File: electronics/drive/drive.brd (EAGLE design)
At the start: 35 x 25 mm, 11 parts, among them IC1 MEGA8-AI, IC2 MAX1483ESA, J1 AVR_SPI_PRG_6NS

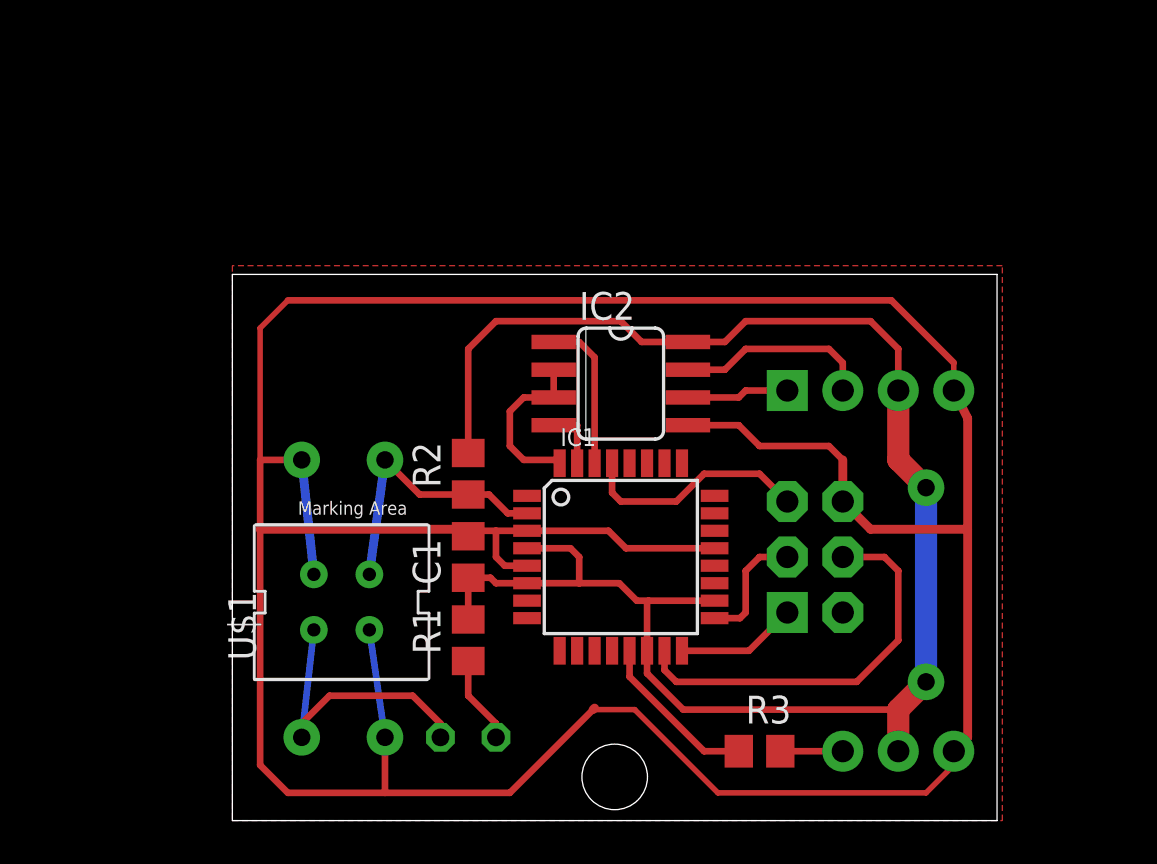
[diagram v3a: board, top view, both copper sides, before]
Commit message: Editing the board based on the build experiences :-)
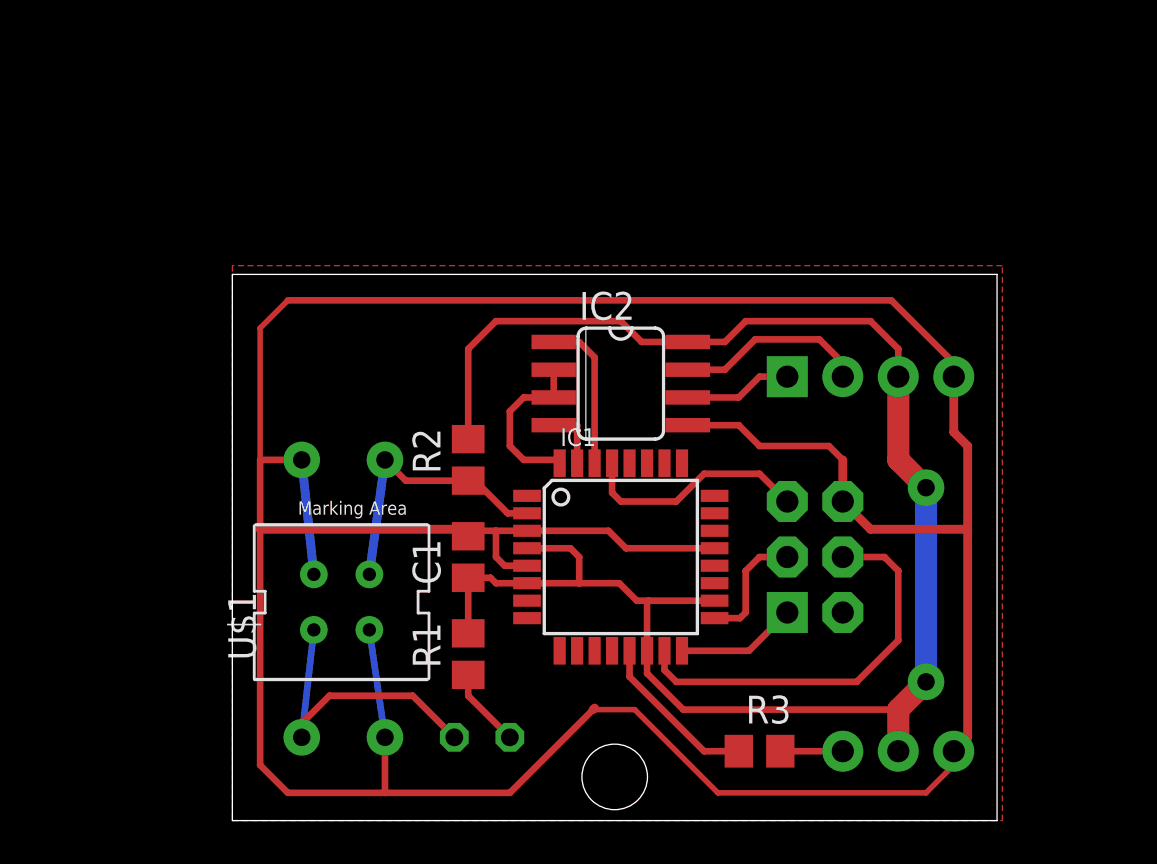
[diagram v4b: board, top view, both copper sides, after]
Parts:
- moved JP1 0.64 mm to (25.4, 20.3)
- moved R2 0.64 mm to (10.8, 16.5)
- moved R1 0.64 mm to (10.8, 7.62)
- moved LED1 0.63 mm to (11.4, 3.81)
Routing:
- net +5V: track 80.3 -> 79.6 mm
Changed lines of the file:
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@@
 <attribute name="NAME" x="1.079" y="7.333" size="1.27" layer="25" ratio="10" rot="R90"/>
 </element>
-<element name="LED1" library="led" package="LED3MM" value="3MM RED / 20mA, 1.8V" x="10.795" y="3.81" rot="MR0"/>
-<element name="R1" library="rcl" package="R0805" value="200" x="10.795" y="8.255" rot="R90"/>
+<element name="LED1" library="led" package="LED3MM" value="3MM RED / 20mA, 1.8V" x="11.43" y="3.81" rot="MR0"/>
+<element name="R1" library="rcl" package="R0805" value="200" x="10.795" y="7.62" rot="R90"/>
 <element name="C1" library="rcl" package="C0805" value="100nF" x="10.795" y="12.065" rot="R90"/>
-<element name="JP1" library="SparkFun" package="MOLEX-1X4" value="" x="25.4" y="19.685" rot="MR180"/>
+<element name="JP1" library="SparkFun" package="MOLEX-1X4" value="" x="25.4" y="20.32" rot="MR180"/>
 <element name="JP2" library="SparkFun" package="1X03" value="" x="33.02" y="3.175" rot="MR0"/>
 <element name="IC1" library="atmel" package="TQFP32-08" value="MEGA8-AI" x="17.78" y="12.065">
@@
 </element>
 <element name="J1" library="SparkFun" package="2X3-NS" value="AVR_SPI_PRG_6NS" x="26.67" y="12.065" rot="MR90"/>
-<element name="R2" library="rcl" package="R0805" value="12k" x="10.795" y="15.875" rot="R90"/>
+<element name="R2" library="rcl" package="R0805" value="12k" x="10.795" y="16.51" rot="R90"/>
 <element name="R3" library="rcl" package="R0805" value="1k" x="24.13" y="3.175"/>
 </elements>
@@
 <wire x1="18.415" y1="5.08" x2="22.225" y2="1.27" width="0.254" layer="1"/>
 <wire x1="16.51" y1="5.08" x2="18.415" y2="5.08" width="0.254" layer="1"/>
-<wire x1="33.02" y1="20.955" x2="33.02" y2="19.685" width="0.254" layer="1"/>
+<wire x1="33.02" y1="20.955" x2="33.02" y2="20.32" width="0.254" layer="1"/>
 <wire x1="30.1625" y1="23.8125" x2="33.02" y2="20.955" width="0.3048" layer="1"/>
 <wire x1="2.54" y1="23.8125" x2="30.1625" y2="23.8125" width="0.3048" layer="1"/>
@@
 <wire x1="33.02" y1="3.175" x2="33.655" y2="3.81" width="0.4064" layer="1"/>
 <wire x1="33.655" y1="3.81" x2="33.655" y2="13.335" width="0.4064" layer="1"/>
-<wire x1="33.655" y1="13.335" x2="33.655" y2="18.415" width="0.4064" layer="1"/>
-<wire x1="33.655" y1="18.415" x2="33.02" y2="19.685" width="0.4064" layer="1"/>
+<wire x1="33.655" y1="13.335" x2="33.655" y2="17.145" width="0.4064" layer="1"/>
+<wire x1="33.655" y1="17.145" x2="33.02" y2="17.78" width="0.4064" layer="1"/>
+<wire x1="33.02" y1="17.78" x2="33.02" y2="20.32" width="0.4064" layer="1"/>
 <wire x1="13.4874" y1="11.665" x2="12.465" y2="11.665" width="0.3048" layer="1"/>
 <wire x1="12.465" y1="11.665" x2="12.065" y2="12.065" width="0.3048" layer="1"/>
@@
 <via x="6.985" y="16.51" extent="1-16" drill="0.8" diameter="1.6764"/>
 <wire x1="13.4874" y1="14.065" x2="12.605" y2="14.065" width="0.3048" layer="1"/>
-<wire x1="12.605" y1="14.065" x2="11.745" y2="14.925" width="0.3048" layer="1"/>
-<wire x1="10.795" y1="14.925" x2="11.745" y2="14.925" width="0.3048" layer="1"/>
-<wire x1="10.795" y1="14.925" x2="8.57" y2="14.925" width="0.3048" layer="1"/>
-<wire x1="8.57" y1="14.925" x2="6.985" y2="16.51" width="0.3048" layer="1"/>
+<wire x1="12.605" y1="14.065" x2="11.11" y2="15.56" width="0.3048" layer="1"/>
+<wire x1="10.795" y1="15.56" x2="11.11" y2="15.56" width="0.3048" layer="1"/>
+<wire x1="10.795" y1="15.56" x2="7.935" y2="15.56" width="0.3048" layer="1"/>
+<wire x1="7.935" y1="15.56" x2="6.985" y2="16.51" width="0.3048" layer="1"/>
 </signal>
 <signal name="N$2">
@@
 <contactref element="LED1" pad="K"/>
 <wire x1="3.73" y1="8.73" x2="3.175" y2="3.81" width="0.3048" layer="16"/>
-<wire x1="9.525" y1="3.81" x2="9.525" y2="4.445" width="0.3048" layer="1"/>
-<wire x1="9.525" y1="4.445" x2="8.255" y2="5.715" width="0.3048" layer="1"/>
 <via x="3.175" y="3.81" extent="1-16" drill="0.8" diameter="1.6764"/>
 <wire x1="3.175" y1="3.81" x2="3.175" y2="4.445" width="0.3048" layer="1"/>
 <wire x1="3.175" y1="4.445" x2="4.445" y2="5.715" width="0.3048" layer="1"/>
 <wire x1="4.445" y1="5.715" x2="8.255" y2="5.715" width="0.3048" layer="1"/>
+<wire x1="8.255" y1="5.715" x2="10.16" y2="3.81" width="0.3048" layer="1"/>
 </signal>
 <signal name="+5V">
@@
 <wire x1="19.05" y1="10.065" x2="18.98" y2="9.995" width="0.3048" layer="1"/>
 <wire x1="30.48" y1="4.1275" x2="30.48" y2="3.175" width="0.4064" layer="1"/>
-<wire x1="30.48" y1="19.685" x2="30.48" y2="20.32" width="0.4064" layer="1"/>
 <wire x1="18.98" y1="7.7724" x2="18.98" y2="6.7375" width="0.3048" layer="1"/>
 <via x="31.75" y="6.35" extent="1-16" drill="0.8" diameter="1.6764"/>
@@
 <wire x1="30.48" y1="5.08" x2="30.48" y2="3.175" width="1.016" layer="1"/>
 <wire x1="31.75" y1="6.35" x2="30.48" y2="5.08" width="1.016" layer="1"/>
-<wire x1="30.48" y1="19.685" x2="30.48" y2="16.51" width="1.016" layer="1"/>
+<wire x1="30.48" y1="20.32" x2="30.48" y2="16.51" width="1.016" layer="1"/>
 <wire x1="30.48" y1="16.51" x2="31.75" y2="15.24" width="1.016" layer="1"/>
 <contactref element="R1" pad="2"/>
@@
 <wire x1="10.795" y1="11.115" x2="11.815" y2="11.115" width="0.3048" layer="1"/>
 <wire x1="11.815" y1="11.115" x2="12.065" y2="10.865" width="0.3048" layer="1"/>
-<wire x1="10.795" y1="9.205" x2="10.795" y2="11.115" width="0.3048" layer="1"/>
+<wire x1="10.795" y1="8.57" x2="10.795" y2="11.115" width="0.3048" layer="1"/>
 <wire x1="20.6375" y1="5.08" x2="30.48" y2="5.08" width="0.3048" layer="1"/>
 <wire x1="12.065" y1="22.86" x2="10.795" y2="21.59" width="0.3048" layer="1"/>
-<wire x1="10.795" y1="21.59" x2="10.795" y2="16.825" width="0.3048" layer="1"/>
+<wire x1="10.795" y1="21.59" x2="10.795" y2="17.46" width="0.3048" layer="1"/>
 <wire x1="12.065" y1="22.86" x2="17.78" y2="22.86" width="0.3048" layer="1"/>
 <wire x1="17.78" y1="22.86" x2="18.7325" y2="21.9075" width="0.3048" layer="1"/>
@@
 <wire x1="23.495" y1="22.86" x2="29.21" y2="22.86" width="0.3048" layer="1"/>
 <wire x1="29.21" y1="22.86" x2="30.48" y2="21.59" width="0.3048" layer="1"/>
-<wire x1="30.48" y1="21.59" x2="30.48" y2="19.685" width="0.3048" layer="1"/>
+<wire x1="30.48" y1="21.59" x2="30.48" y2="20.32" width="0.3048" layer="1"/>
 </signal>
 <signal name="SERVO">
@@
 <contactref element="JP1" pad="1"/>
 <wire x1="20.8534" y1="19.3675" x2="23.1775" y2="19.3675" width="0.3048" layer="1"/>
-<wire x1="23.1775" y1="19.3675" x2="23.495" y2="19.685" width="0.3048" layer="1"/>
-<wire x1="23.495" y1="19.685" x2="25.4" y2="19.685" width="0.3048" layer="1"/>
+<wire x1="23.1775" y1="19.3675" x2="24.13" y2="20.32" width="0.3048" layer="1"/>
+<wire x1="24.13" y1="20.32" x2="25.4" y2="20.32" width="0.3048" layer="1"/>
 </signal>
 <signal name="D-">
@@
 <contactref element="JP1" pad="2"/>
 <wire x1="20.8534" y1="20.6375" x2="22.5425" y2="20.6375" width="0.3048" layer="1"/>
-<wire x1="22.5425" y1="20.6375" x2="23.495" y2="21.59" width="0.3048" layer="1"/>
-<wire x1="23.495" y1="21.59" x2="27.305" y2="21.59" width="0.3048" layer="1"/>
-<wire x1="27.305" y1="21.59" x2="27.94" y2="20.955" width="0.3048" layer="1"/>
-<wire x1="27.94" y1="20.955" x2="27.94" y2="19.685" width="0.3048" layer="1"/>
+<wire x1="22.5425" y1="20.6375" x2="23.93" y2="22.025" width="0.3048" layer="1"/>
+<wire x1="23.93" y1="22.025" x2="26.87" y2="22.025" width="0.3048" layer="1"/>
+<wire x1="26.87" y1="22.025" x2="27.94" y2="20.955" width="0.3048" layer="1"/>
+<wire x1="27.94" y1="20.955" x2="27.94" y2="20.32" width="0.3048" layer="1"/>
 </signal>
 <signal name="TXEN">
@@
 <contactref element="LED1" pad="A"/>
 <contactref element="R1" pad="1"/>
-<wire x1="10.795" y1="7.305" x2="10.795" y2="5.715" width="0.3048" layer="1"/>
-<wire x1="10.795" y1="5.715" x2="12.065" y2="4.445" width="0.3048" layer="1"/>
-<wire x1="12.065" y1="4.445" x2="12.065" y2="3.81" width="0.3048" layer="1"/>
+<wire x1="10.795" y1="6.67" x2="10.795" y2="5.715" width="0.3048" layer="1"/>
+<wire x1="10.795" y1="5.715" x2="12.7" y2="3.81" width="0.3048" layer="1"/>
 </signal>
 <signal name="N$1">

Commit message: First attempt on making the drive board compatible with my soldering skills.
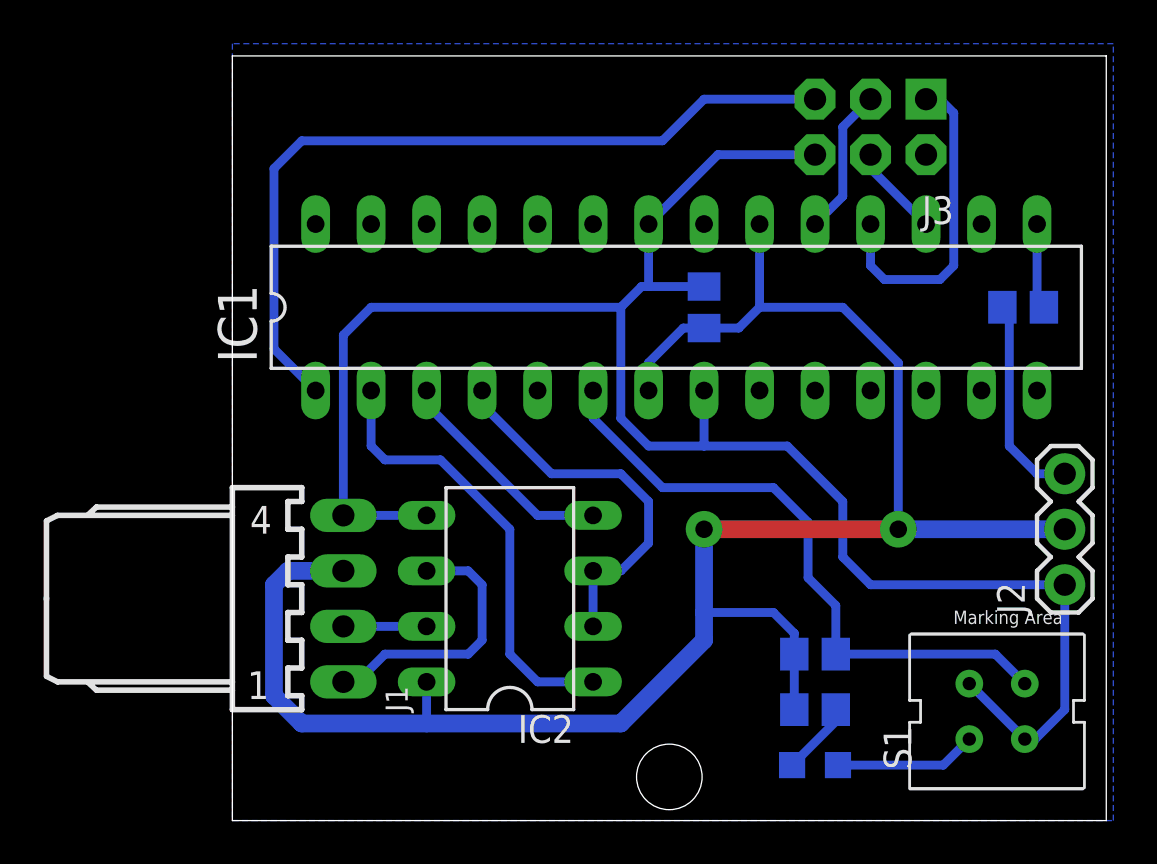
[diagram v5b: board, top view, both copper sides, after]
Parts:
- removed JP1: (no value), SparkFun:MOLEX-1X4
- removed JP2: (no value), SparkFun:1X03
- removed U$1: CNY70, cny70:4
- added J2: (no value), SparkFun:1X03
- added J3: AVR_SPI_PRG_6NS, SparkFun:2X3-NS
- added S1: CNY70, cny70:4
- IC1: value MEGA8-AI -> MEGA8-P; device atmel:TQFP32-08 -> atmel:DIL28-3
- IC2: value MAX1483ESA -> MAX481CPA; device maxim:SO08 -> maxim:DIL08
- J1: value AVR_SPI_PRG_6NS -> 22-05-7048-04; device SparkFun:2X3-NS -> con-molex:7395-04
- LED1: device led:LED3MM -> led:CHIP-LED0805
- moved R3 23.6 mm to (36.2, 23.5), flipped to the bottom
- moved J1 21.7 mm to (5.08, 10.2), flipped to the top, turned to 270 degrees
- moved R2 18.2 mm to (26.7, 7.62), flipped to the bottom, turned to 0 degrees
- moved R1 16.1 mm to (26.7, 5.08), flipped to the bottom, turned to 0 degrees
- moved C1 15.7 mm to (21.6, 23.5), flipped to the bottom
- moved LED1 15.3 mm to (26.7, 2.54), turned to 90 degrees
- moved IC1 11.7 mm to (20.3, 23.5)
- moved IC2 11.1 mm to (12.7, 10.2), turned to 90 degrees
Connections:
- net +5V: now also IC1.20, IC1.7, J1.3, J2.2; no longer IC1.14, IC1.18, IC1.4, IC1.6, JP1.3, JP2.2
- net D+: now also J1.1; no longer JP1.1
- net D-: now also J1.2; no longer JP1.2
- net GND: now also IC1.22, IC1.8, J1.4, J2.1, J3.6, S1.E, S1.K; no longer IC1.21, IC1.3, IC1.5, J1.6, JP1.4, JP2.1, U$1.E, U$1.K
- net MISO: now also IC1.18, J3.1; no longer IC1.16, J1.1
- net MOSI: now also IC1.17, J3.4; no longer IC1.15, J1.4
- net N$1: now also J2.3; no longer JP2.3
- net N$2: now also LED1.C, S1.A; no longer LED1.K, U$1.A
- net RESET: now also IC1.1, J3.5; no longer IC1.29, J1.5
- net RX: now also IC1.2; no longer IC1.30
- net SCK: now also IC1.19, J3.3; no longer IC1.17, J1.3
- net SENSOR: now also IC1.6, S1.C; no longer IC1.2, U$1.C
- net SERVO: now also IC1.15; no longer IC1.13
- net TX: now also IC1.3; no longer IC1.31
- net TXEN: now also IC1.4; no longer IC1.32
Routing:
- net GND: track 163.4 -> 85.6 mm, vias 2 -> 0
- net RESET: track 10.6 -> 37.0 mm
- net SENSOR: track 12.8 -> 28.9 mm, vias 1 -> 0
- net MOSI: track 18.6 -> 4.23 mm
- net RX: track 7.01 -> 20.5 mm
- net TXEN: track 7.73 -> 17.6 mm
- net MISO: track 5.55 -> 14.8 mm
- net +5V: track 79.6 -> 88.1 mm
- net TX: track 2.81 -> 10.4 mm
- net D+: track 4.94 -> 12.5 mm
- net N$2: track 13.9 -> 6.50 mm, vias 1 -> 0
- net N$1: track 2.86 -> 9.55 mm
- net D-: track 8.74 -> 3.81 mm
- net SERVO: track 7.60 -> 3.94 mm
- net SCK: track 5.60 -> 6.77 mm
- added copper zone on layer 16, net GND
- removed copper zone on layer 1, net GND
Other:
- board size 35 x 25 mm -> 40 x 35 mm
